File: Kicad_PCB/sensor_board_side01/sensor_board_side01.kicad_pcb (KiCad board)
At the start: 2 copper layers, 30 x 10 mm, 1 part, among them J1 Conn_01x06_Female

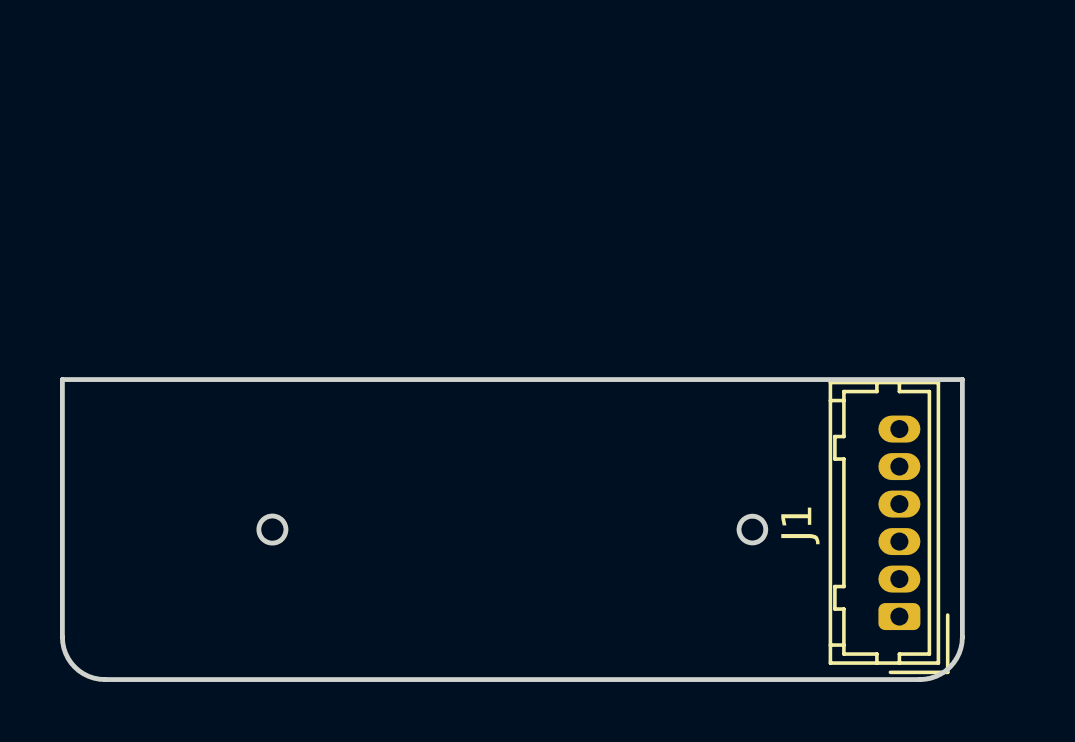
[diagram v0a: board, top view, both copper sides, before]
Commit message: ohmmeter circuit
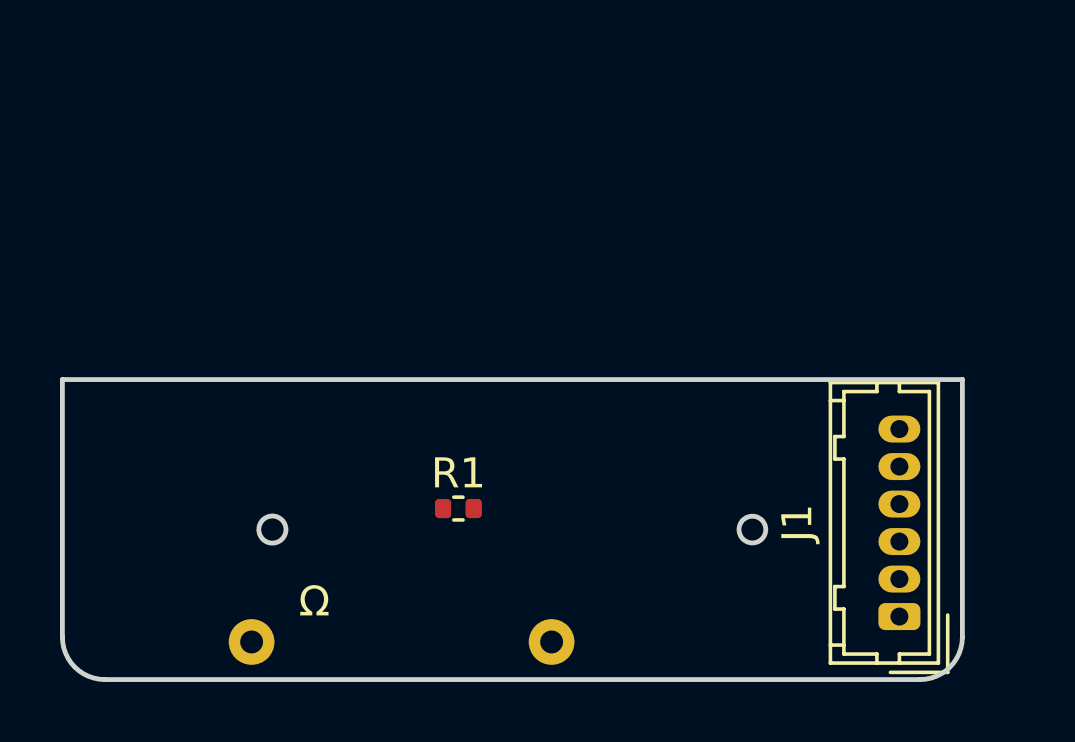
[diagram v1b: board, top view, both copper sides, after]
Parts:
- added R1: 10, Resistor_SMD:R_0402_1005Metric, F.Cu at (155.0, 137.4)
- added U1: ohmmetr, ohm_metr:ohm_metr, F.Cu at (148.1, 141.8)
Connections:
- J1 pad 1: unconnected-(J1-Pad1) -> VDD
- J1 pad 2: unconnected-(J1-Pad2) -> Net-(J1-Pad2)
- J1 pad 6: unconnected-(J1-Pad6) -> GND
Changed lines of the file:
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@@
   )
   (net 0 "")
-  (net 1 "unconnected-(J1-Pad1)")
-  (net 2 "unconnected-(J1-Pad2)")
+  (net 1 "VDD")
+  (net 2 "Net-(J1-Pad2)")
   (net 3 "unconnected-(J1-Pad3)")
   (net 4 "unconnected-(J1-Pad4)")
   (net 5 "unconnected-(J1-Pad5)")
-  (net 6 "unconnected-(J1-Pad6)")
+  (net 6 "GND")
+  (footprint "Resistor_SMD:R_0402_1005Metric" (layer "F.Cu")
+    (at 155 137.4)
+    (descr "Resistor SMD 0402 (1005 Metric), square (rectangular) end terminal, IPC_7351 nominal, (Body size source: IPC-SM-782 page 72, https://www.pcb-3d.com/wordpress/wp-content/uploads/ipc-sm-782a_amendment_1_and_2.pdf), generated with kicad-footprint-generator")
+    (tags "resistor")
+    (property "Sheetfile" "sensor_board_side01.kicad_sch")
+    (property "Sheetname" "")
+    (attr smd)
+    (fp_text reference "R1" (at 0 -1.17) (layer "F.SilkS")
+      (effects (font (size 1 1) (thickness 0.15)))
+    )
+    (fp_text value "10" (at 0 1.17) (layer "F.Fab")
+      (effects (font (size 1 1) (thickness 0.15)))
+    )
+    (fp_text user "${REFERENCE}" (at 0 0) (layer "F.Fab")
+      (effects (font (size 0.26 0.26) (thickness 0.04)))
+    )
+    (fp_line (start -0.153641 0.38) (end 0.153641 0.38) (layer "F.SilkS") (width 0.12))
+    (fp_line (start -0.153641 -0.38) (end 0.153641 -0.38) (layer "F.SilkS") (width 0.12))
+    (fp_line (start 0.93 -0.47) (end 0.93 0.47) (layer "F.CrtYd") (width 0.05))
+    (fp_line (start -0.93 0.47) (end -0.93 -0.47) (layer "F.CrtYd") (width 0.05))
+    (fp_line (start 0.93 0.47) (end -0.93 0.47) (layer "F.CrtYd") (width 0.05))
+    (fp_line (start -0.93 -0.47) (end 0.93 -0.47) (layer "F.CrtYd") (width 0.05))
+    (fp_line (start -0.525 0.27) (end -0.525 -0.27) (layer "F.Fab") (width 0.1))
+    (fp_line (start -0.525 -0.27) (end 0.525 -0.27) (layer "F.Fab") (width 0.1))
+    (fp_line (start 0.525 -0.27) (end 0.525 0.27) (layer "F.Fab") (width 0.1))
+    (fp_line (start 0.525 0.27) (end -0.525 0.27) (layer "F.Fab") (width 0.1))
+    (pad "1" smd roundrect (at -0.51 0) (size 0.54 0.64) (layers "F.Cu" "F.Paste" "F.Mask") (roundrect_rratio 0.25)
+      (net 1 "VDD") (pintype "passive"))
+    (pad "2" smd roundrect (at 0.51 0) (size 0.54 0.64) (layers "F.Cu" "F.Paste" "F.Mask") (roundrect_rratio 0.25)
+      (net 2 "Net-(J1-Pad2)") (pintype "passive"))
+    (model "${KICAD6_3DMODEL_DIR}/Resistor_SMD.3dshapes/R_0402_1005Metric.wrl"
+      (offset (xyz 0 0 0))
+      (scale (xyz 1 1 1))
+      (rotate (xyz 0 0 0))
+    )
+  )
   (footprint "Connector_Hirose:Hirose_DF13-06P-1.25DSA_1x06_P1.25mm_Vertical" (layer "F.Cu")
     (at 169.7 141 90)
@@
     (fp_line (start -1.45 -2.2) (end -1.45 1.2) (layer "F.Fab") (width 0.1))
     (pad "1" thru_hole roundrect (at 0 0 90) (size 0.9 1.4) (drill 0.6) (layers *.Cu *.Mask) (roundrect_rratio 0.25)
-      (net 1 "unconnected-(J1-Pad1)") (pinfunction "Pin_1") (pintype "passive"))
+      (net 1 "VDD") (pinfunction "Pin_1") (pintype "passive"))
     (pad "2" thru_hole oval (at 1.25 0 90) (size 0.9 1.4) (drill 0.6) (layers *.Cu *.Mask)
-      (net 2 "unconnected-(J1-Pad2)") (pinfunction "Pin_2") (pintype "passive"))
+      (net 2 "Net-(J1-Pad2)") (pinfunction "Pin_2") (pintype "passive"))
     (pad "3" thru_hole oval (at 2.5 0 90) (size 0.9 1.4) (drill 0.6) (layers *.Cu *.Mask)
       (net 3 "unconnected-(J1-Pad3)") (pinfunction "Pin_3") (pintype "passive"))
@@
       (net 5 "unconnected-(J1-Pad5)") (pinfunction "Pin_5") (pintype "passive"))
     (pad "6" thru_hole oval (at 6.25 0 90) (size 0.9 1.4) (drill 0.6) (layers *.Cu *.Mask)
-      (net 6 "unconnected-(J1-Pad6)") (pinfunction "Pin_6") (pintype "passive"))
+      (net 6 "GND") (pinfunction "Pin_6") (pintype "passive"))
     (model "${KICAD6_3DMODEL_DIR}/Connector_Hirose.3dshapes/Hirose_DF13-06P-1.25DSA_1x06_P1.25mm_Vertical.wrl"
       (offset (xyz 0 0 0))
@@
     )
   )
+  (footprint "ohm_metr:ohm_metr" (layer "F.Cu")
+    (at 148.107 141.847)
+    (property "Sheetfile" "sensor_board_side01.kicad_sch")
+    (property "Sheetname" "")
+    (attr through_hole)
+    (fp_text reference "U1" (at -1 -2 unlocked) (layer "F.SilkS") hide
+      (effects (font (size 1 1) (thickness 0.15)))
+    )
+    (fp_text value "ohmmetr" (at 5.693 -0.247 unlocked) (layer "F.Fab")
+      (effects (font (size 1 1) (thickness 0.15)))
+    )
+    (fp_text user "Ω" (at 2.093 -1.347 unlocked) (layer "F.SilkS")
+      (effects (font (size 1 1) (thickness 0.15)))
+    )
+    (fp_text user "${REFERENCE}" (at 10 -3 unlocked) (layer "F.Fab") hide
+      (effects (font (size 1 1) (thickness 0.15)))
+    )
+    (pad "1" thru_hole circle (at 0 0) (size 1.524 1.524) (drill 0.762) (layers *.Cu *.Mask)
+      (net 2 "Net-(J1-Pad2)") (pinfunction "pr") (pintype "input"))
+    (pad "2" thru_hole circle (at 10 0) (size 1.524 1.524) (drill 0.762) (layers *.Cu *.Mask)
+      (net 6 "GND") (pinfunction "pr0") (pintype "input"))
+  )
   (gr_arc (start 143.214214 143.1) (mid 142.214214 142.685786) (end 141.8 141.685786) (layer "Edge.Cuts") (width 0.16))

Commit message: Sensor Board Schematic
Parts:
- added C1: 1uF, Capacitor_SMD:C_0805_2012Metric, F.Cu at (164.3, 136.0)
- added C2: 0.1uF, Capacitor_SMD:C_0805_2012Metric, F.Cu at (151.0, 138.9)
- added C3: 10nF, Capacitor_SMD:C_0805_2012Metric, F.Cu at (158.5, 136.3)
- added R2: 1k, Resistor_SMD:R_0402_1005Metric, F.Cu at (158.5, 138.4)
- added R3: 100k, Resistor_SMD:R_0402_1005Metric, F.Cu at (154.8, 137.2)
- added R4: 1M, Resistor_SMD:R_0402_1005Metric, F.Cu at (161.5, 136.1)
- added R5: 10k, Resistor_SMD:R_0402_1005Metric, F.Cu at (154.4, 138.7)
- added U2: AT42QT1012-M, Package_DFN_QFN:DFN-8-1EP_2x2mm_P0.5mm_EP0.9x1.5mm, F.Cu at (151.7, 136.0)
- added U3: sensor, cup_toch:toch_sens, F.Cu at (168.7, 141.1)
- J1: moved to B.Cu
- moved J1 25.2 mm to (144.5, 141.0)
- moved R1 7.03 mm to (162.0, 138.0)
- moved U1 4.49 mm to (152.6, 141.8)
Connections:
- J1 pad 3: unconnected-(J1-Pad3) -> Net-(J1-Pad3)

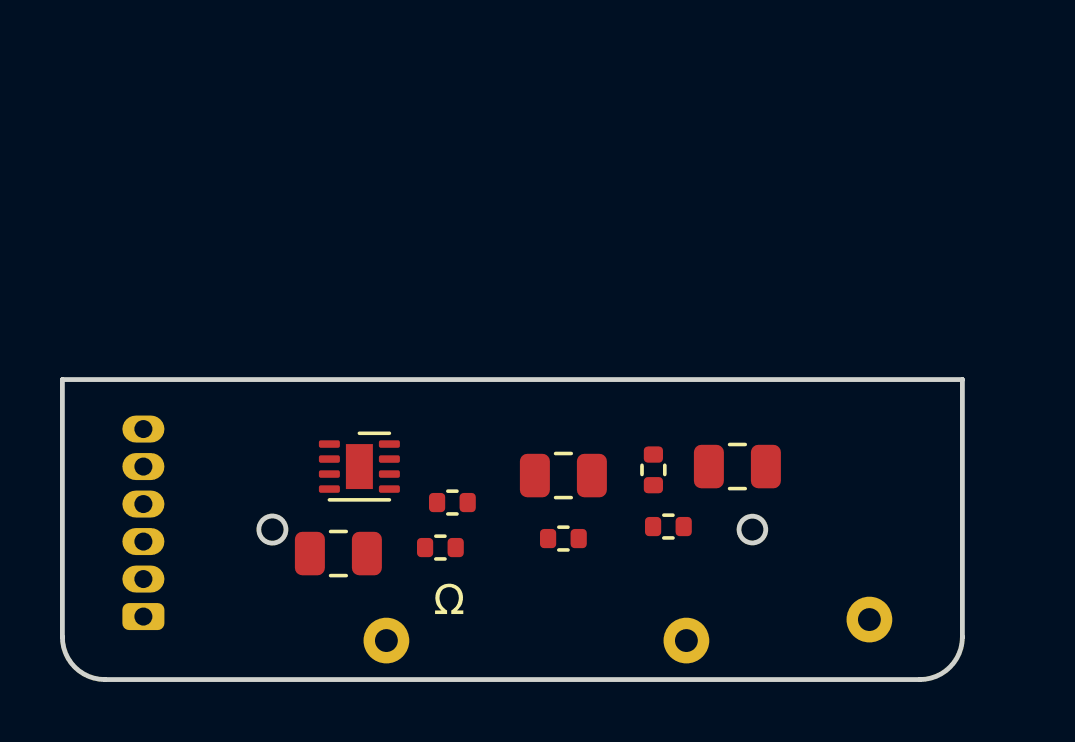
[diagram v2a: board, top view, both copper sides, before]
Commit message: conic spring in sockets with PCB
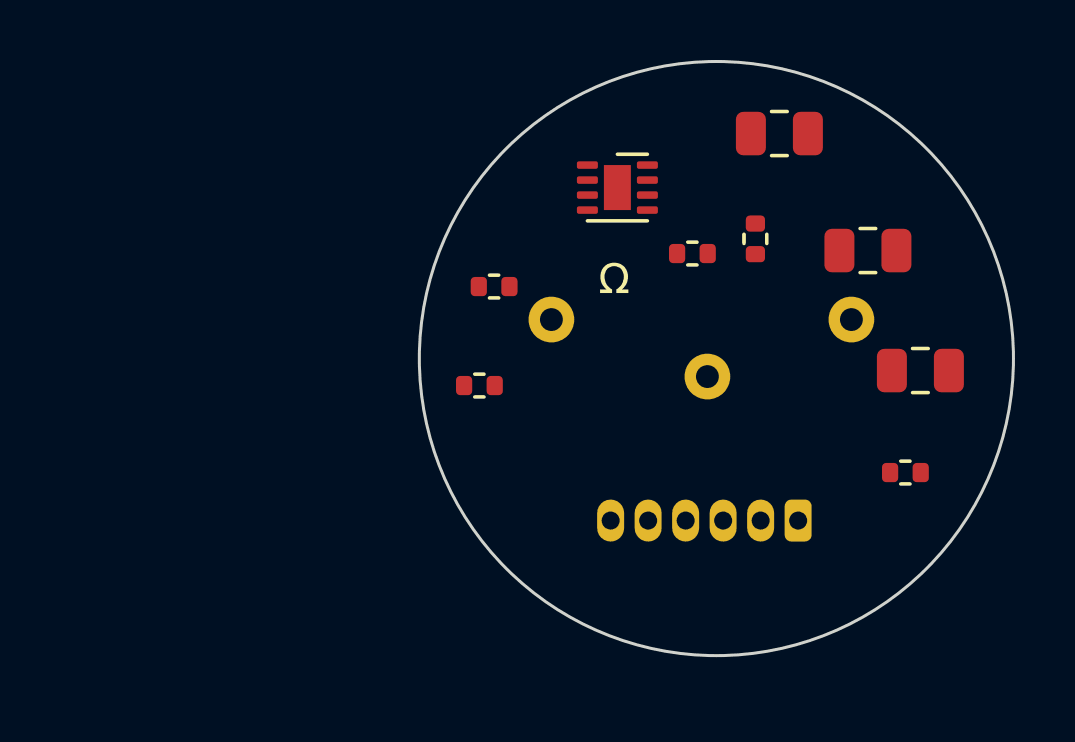
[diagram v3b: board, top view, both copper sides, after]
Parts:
- moved J1 22.1 mm to (166.3, 137.8), turned to 180 degrees
- moved C2 20.3 mm to (165.7, 124.9)
- moved U2 12.7 mm to (160.3, 126.7)
- moved C3 12.6 mm to (168.7, 128.8)
- moved U1 12.0 mm to (158.1, 131.1)
- moved R2 11.6 mm to (169.9, 136.2)
- moved U3 9.73 mm to (163.3, 133.0)
- moved R1 9.14 mm to (162.8, 128.9)
- moved R4 8.42 mm to (164.9, 128.4)
- moved R3 7.33 mm to (156.2, 130.0)
- moved C1 6.89 mm to (170.4, 132.8)
- moved R5 5.55 mm to (155.7, 133.3)
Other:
- board size 30 x 10 mm -> 19.8 x 19.8 mm
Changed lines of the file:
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@@
   (net 11 "Net-(R5-Pad2)")
   (footprint "Resistor_SMD:R_0402_1005Metric" (layer "F.Cu")
-    (at 154.8 137.2)
+    (at 156.19 130)
     (descr "Resistor SMD 0402 (1005 Metric), square (rectangular) end terminal, IPC_7351 nominal, (Body size source: IPC-SM-782 page 72, https://www.pcb-3d.com/wordpress/wp-content/uploads/ipc-sm-782a_amendment_1_and_2.pdf), generated with kicad-footprint-generator")
     (tags "resistor")
@@
   )
   (footprint "Resistor_SMD:R_0402_1005Metric" (layer "F.Cu")
-    (at 158.5 138.4)
+    (at 169.9 136.2)
     (descr "Resistor SMD 0402 (1005 Metric), square (rectangular) end terminal, IPC_7351 nominal, (Body size source: IPC-SM-782 page 72, https://www.pcb-3d.com/wordpress/wp-content/uploads/ipc-sm-782a_amendment_1_and_2.pdf), generated with kicad-footprint-generator")
     (tags "resistor")
@@
   )
   (footprint "Capacitor_SMD:C_0805_2012Metric" (layer "F.Cu")
-    (at 158.5 136.3 180)
+    (at 168.65 128.8 180)
     (descr "Capacitor SMD 0805 (2012 Metric), square (rectangular) end terminal, IPC_7351 nominal, (Body size source: IPC-SM-782 page 76, https://www.pcb-3d.com/wordpress/wp-content/uploads/ipc-sm-782a_amendment_1_and_2.pdf, https://docs.google.com/spreadsheets/d/1BsfQQcO9C6DZCsRaXUlFlo91Tg2WpOkGARC1WS5S8t0/edit?usp=sharing), generated with kicad-footprint-generator")
     (tags "capacitor")
@@
   )
   (footprint "cup_toch:toch_sens" (layer "F.Cu")
-    (at 168.7 141.1)
+    (at 163.3 133)
     (property "Sheetfile" "sensor_board_side01.kicad_sch")
     (property "Sheetname" "")
@@
   )
   (footprint "Resistor_SMD:R_0402_1005Metric" (layer "F.Cu")
-    (at 162 138)
+    (at 162.8 128.9)
     (descr "Resistor SMD 0402 (1005 Metric), square (rectangular) end terminal, IPC_7351 nominal, (Body size source: IPC-SM-782 page 72, https://www.pcb-3d.com/wordpress/wp-content/uploads/ipc-sm-782a_amendment_1_and_2.pdf), generated with kicad-footprint-generator")
     (tags "resistor")
@@
   )
   (footprint "Package_DFN_QFN:DFN-8-1EP_2x2mm_P0.5mm_EP0.9x1.5mm" (layer "F.Cu")
-    (at 151.7 136)
+    (at 160.3 126.7)
     (descr "DFN, 8 Pin (http://ww1.microchip.com/downloads/en/DeviceDoc/Atmel-8127-AVR-8-bit-Microcontroller-ATtiny4-ATtiny5-ATtiny9-ATtiny10_Datasheet.pdf), generated with kicad-footprint-generator ipc_noLead_generator.py")
     (tags "DFN NoLead")
@@
   )
   (footprint "Capacitor_SMD:C_0805_2012Metric" (layer "F.Cu")
-    (at 164.3 136 180)
+    (at 170.4 132.8 180)
     (descr "Capacitor SMD 0805 (2012 Metric), square (rectangular) end terminal, IPC_7351 nominal, (Body size source: IPC-SM-782 page 76, https://www.pcb-3d.com/wordpress/wp-content/uploads/ipc-sm-782a_amendment_1_and_2.pdf, https://docs.google.com/spreadsheets/d/1BsfQQcO9C6DZCsRaXUlFlo91Tg2WpOkGARC1WS5S8t0/edit?usp=sharing), generated with kicad-footprint-generator")
     (tags "capacitor")
@@
   )
   (footprint "Capacitor_SMD:C_0805_2012Metric" (layer "F.Cu")
-    (at 151 138.9 180)
+    (at 165.7 124.9 180)
     (descr "Capacitor SMD 0805 (2012 Metric), square (rectangular) end terminal, IPC_7351 nominal, (Body size source: IPC-SM-782 page 76, https://www.pcb-3d.com/wordpress/wp-content/uploads/ipc-sm-782a_amendment_1_and_2.pdf, https://docs.google.com/spreadsheets/d/1BsfQQcO9C6DZCsRaXUlFlo91Tg2WpOkGARC1WS5S8t0/edit?usp=sharing), generated with kicad-footprint-generator")
     (tags "capacitor")
@@
   )
   (footprint "ohm_metr:ohm_metr" (layer "F.Cu")
-    (at 152.6 141.8)
+    (at 158.1 131.1)
     (property "Sheetfile" "sensor_board_side01.kicad_sch")
     (property "Sheetname" "")
@@
   )
   (footprint "Resistor_SMD:R_0402_1005Metric" (layer "F.Cu")
-    (at 161.5 136.11 90)
+    (at 164.9 128.41 90)
     (descr "Resistor SMD 0402 (1005 Metric), square (rectangular) end terminal, IPC_7351 nominal, (Body size source: IPC-SM-782 page 72, https://www.pcb-3d.com/wordpress/wp-content/uploads/ipc-sm-782a_amendment_1_and_2.pdf), generated with kicad-footprint-generator")
     (tags "resistor")
@@
   )
   (footprint "Resistor_SMD:R_0402_1005Metric" (layer "F.Cu")
-    (at 154.4 138.7 180)
+    (at 155.7 133.3 180)
     (descr "Resistor SMD 0402 (1005 Metric), square (rectangular) end terminal, IPC_7351 nominal, (Body size source: IPC-SM-782 page 72, https://www.pcb-3d.com/wordpress/wp-content/uploads/ipc-sm-782a_amendment_1_and_2.pdf), generated with kicad-footprint-generator")
     (tags "resistor")
@@
   )
   (footprint "Connector_Hirose:Hirose_DF13-06P-1.25DSA_1x06_P1.25mm_Vertical" (layer "B.Cu")
-    (at 144.5 141 90)
+    (at 166.325 137.8 180)
     (descr "Hirose DF13 through hole, DF13-06P-1.25DSA, 6 Pins per row (https://www.hirose.com/product/en/products/DF13/DF13-2P-1.25DSA%2850%29/), generated with kicad-footprint-generator")
     (tags "connector Hirose DF13 vertical")
@@
     (property "Sheetname" "")
     (attr through_hole)
-    (fp_text reference "J1" (at 3.12 3.4 90) (layer "B.SilkS") hide
+    (fp_text reference "J1" (at 3.12 3.4) (layer "B.SilkS") hide
       (effects (font (size 1 1) (thickness 0.15)) (justify mirror))
     )
-    (fp_text value "Conn_01x06_Female" (at 3.12 -2.4 90) (layer "B.Fab") hide
+    (fp_text value "Conn_01x06_Female" (at 3.12 -2.4) (layer "B.Fab") hide
       (effects (font (size 1 1) (thickness 0.15)) (justify mirror))
     )
-    (fp_text user "${REFERENCE}" (at 3.12 1.5 90) (layer "B.Fab") hide
+    (fp_text user "${REFERENCE}" (at 3.12 1.5) (layer "B.Fab") hide
       (effects (font (size 1 1) (thickness 0.15)) (justify mirror))
     )
@@
     (fp_line (start 7.7 -1.2) (end 7.7 2.2) (layer "B.Fab") (width 0.1))
     (fp_line (start -1.45 2.2) (end -1.45 -1.2) (layer "B.Fab") (width 0.1))
-    (pad "1" thru_hole roundrect (at 0 0 90) (size 0.9 1.4) (drill 0.6) (layers *.Cu *.Mask) (roundrect_rratio 0.25)
+    (pad "1" thru_hole roundrect (at 0 0 180) (size 0.9 1.4) (drill 0.6) (layers *.Cu *.Mask) (roundrect_rratio 0.25)
       (net 1 "VDD") (pinfunction "Pin_1") (pintype "passive"))
-    (pad "2" thru_hole oval (at 1.25 0 90) (size 0.9 1.4) (drill 0.6) (layers *.Cu *.Mask)
+    (pad "2" thru_hole oval (at 1.25 0 180) (size 0.9 1.4) (drill 0.6) (layers *.Cu *.Mask)
       (net 2 "Net-(C1-Pad1)") (pinfunction "Pin_2") (pintype "passive"))
-    (pad "3" thru_hole oval (at 2.5 0 90) (size 0.9 1.4) (drill 0.6) (layers *.Cu *.Mask)
+    (pad "3" thru_hole oval (at 2.5 0 180) (size 0.9 1.4) (drill 0.6) (layers *.Cu *.Mask)
       (net 10 "Net-(J1-Pad3)") (pinfunction "Pin_3") (pintype "passive"))
-    (pad "4" thru_hole oval (at 3.75 0 90) (size 0.9 1.4) (drill 0.6) (layers *.Cu *.Mask)
+    (pad "4" thru_hole oval (at 3.75 0 180) (size 0.9 1.4) (drill 0.6) (layers *.Cu *.Mask)
       (net 4 "unconnected-(J1-Pad4)") (pinfunction "Pin_4") (pintype "passive"))
-    (pad "5" thru_hole oval (at 5 0 90) (size 0.9 1.4) (drill 0.6) (layers *.Cu *.Mask)
+    (pad "5" thru_hole oval (at 5 0 180) (size 0.9 1.4) (drill 0.6) (layers *.Cu *.Mask)
       (net 5 "unconnected-(J1-Pad5)") (pinfunction "Pin_5") (pintype "passive"))
-    (pad "6" thru_hole oval (at 6.25 0 90) (size 0.9 1.4) (drill 0.6) (layers *.Cu *.Mask)
+    (pad "6" thru_hole oval (at 6.25 0 180) (size 0.9 1.4) (drill 0.6) (layers *.Cu *.Mask)
       (net 6 "GND") (pinfunction "Pin_6") (pintype "passive"))
     (model "${KICAD6_3DMODEL_DIR}/Connector_Hirose.3dshapes/Hirose_DF13-06P-1.25DSA_1x06_P1.25mm_Vertical.wrl"
@@
     )
   )
-  (gr_arc (start 143.214214 143.1) (mid 142.214214 142.685786) (end 141.8 141.685786) (layer "Edge.Cuts") (width 0.16))
-  (gr_circle (center 164.8 138.1) (end 164.354459 138.1) (layer "Edge.Cuts") (width 0.16) (fill none))
-  (gr_arc (start 171.8 141.685786) (mid 171.385785 142.685785) (end 170.385786 143.1) (layer "Edge.Cuts") (width 0.16))
-  (gr_line (start 143.214214 143.1) (end 170.385786 143.1) (layer "Edge.Cuts") (width 0.16))
-  (gr_line (start 171.8 141.685786) (end 171.8 133.1) (layer "Edge.Cuts") (width 0.16))
-  (gr_circle (center 148.8 138.1) (end 148.348091 138.1) (layer "Edge.Cuts") (width 0.16) (fill none))
-  (gr_line (start 171.8 133.1) (end 141.8 133.1) (layer "Edge.Cuts") (width 0.16))
-  (gr_line (start 141.8 133.1) (end 141.8 141.685786) (layer "Edge.Cuts") (width 0.16))
+  (gr_circle (center 163.6 132.4) (end 153.7 132.6) (layer "Edge.Cuts") (width 0.1) (fill none))
 )
